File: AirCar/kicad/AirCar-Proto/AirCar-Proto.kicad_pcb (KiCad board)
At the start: 4 copper layers, 76.2 x 55.9 mm, 22 parts, among them J1 Conn_01x05, J2 Conn_01x20_Socket, J3 Conn_01x06, J4 PJ-102A, J5 Conn_01x20_Socket, SW2 SW_SPDT, U1 Pico, U2 LDL212PU50R, U3 TXU0104BQAR

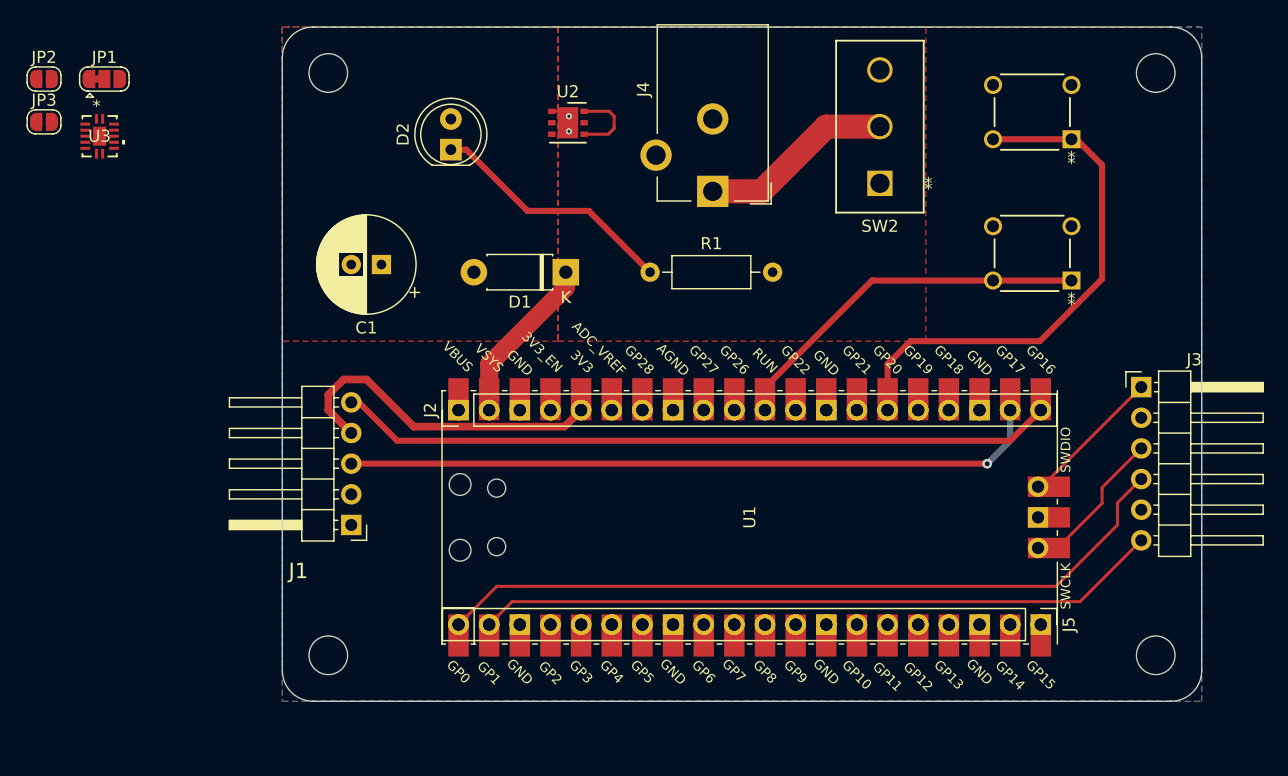
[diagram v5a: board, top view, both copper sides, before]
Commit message: switch to some none through hole parts because SMD is easier...
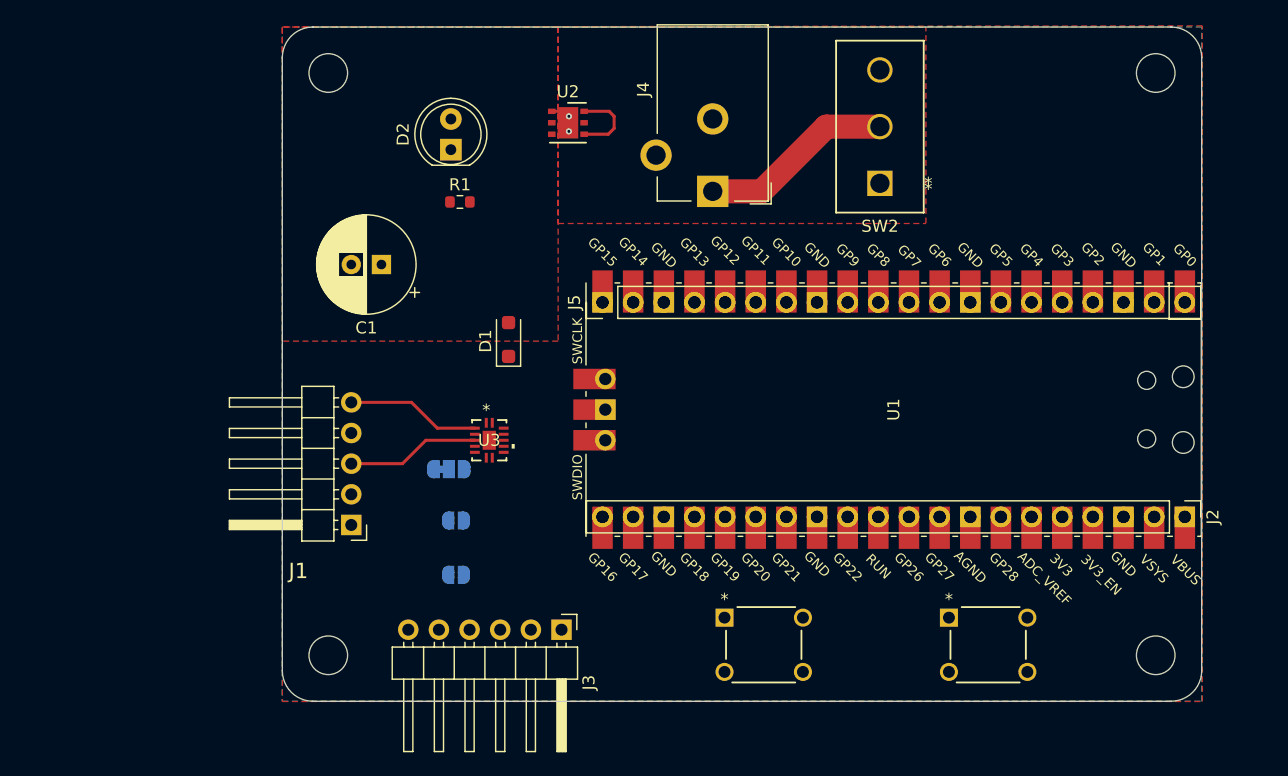
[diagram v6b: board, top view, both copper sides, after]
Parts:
- D1: footprint Diode_THT:D_DO-41_SOD81_P7.62mm_Horizontal -> Diode_SMD:D_SOD-123F
- JP1, JP2, JP3: moved to B.Cu
- R1: footprint Resistor_THT:R_Axial_DIN0207_L6.3mm_D2.5mm_P10.16mm_Horizontal -> Resistor_SMD:R_0603_1608Metric
- moved J2 60.8 mm to (138.3, 142.2), turned to -90 degrees
- moved J3 52.1 mm to (86.6, 151.6), turned to -90 degrees
- moved USER1 51.1 mm to (106.7, 155.1), turned to 0 degrees
- moved JP3 50.7 mm to (77.9, 147.0)
- moved JP2 50.0 mm to (77.9, 142.5)
- moved J5 45.1 mm to (90.0, 124.4), turned to 90 degrees
- moved JP1 43.1 mm to (77.3, 138.2)
- moved U3 41.0 mm to (80.7, 135.8)
- moved Reset1 37.0 mm to (125.3, 155.1), turned to 0 degrees
- moved R1 16.8 mm to (78.2, 116.1)
- moved U1 14.9 mm to (114.2, 133.3), turned to -90 degrees
- moved D1 7.32 mm to (82.2, 127.5), turned to 90 degrees
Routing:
- net /PicoTx: track 62.7 -> 0.00 mm
- net /PicoRx: track 56.9 -> 0.00 mm
- net /Lag: track 59.5 -> 11.1 mm
- net /Lead: track 57.9 -> 11.0 mm, vias 1 -> 0
- net Net-(J2-Pin_15): track 43.9 -> 0.00 mm
- net Net-(J2-Pin_11): track 30.9 -> 0.00 mm
- net (no net): track 27.6 -> 0.00 mm
- net Net-(D2-K): track 20.7 -> 0.00 mm
- net /VSYS: track 14.1 -> 0.00 mm
- net Net-(J3-Pin_3): track 12.7 -> 0.00 mm
- net Net-(J3-Pin_1): track 12.0 -> 0.00 mm
- added copper zone on F.Cu, net /VSYS
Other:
- copper layers 4 -> 2

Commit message: possible rev 0.1 candidate
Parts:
- removed J2, J5: Conn_01x20_Socket, Connector_PinHeader_2.54mm:PinHeader_1x20_P2.54mm_Vertical
- added C2: 0.1uF, Capacitor_SMD:C_0603_1608Metric, F.Cu at (77.3, 140.5)
- moved JP3 10.6 mm to (80.7, 136.8)
- moved JP2 9.17 mm to (80.7, 133.8)
- moved JP1 8.00 mm to (77.2, 130.2)
- moved J1 3.03 mm to (72.2, 142.9)
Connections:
- U1 pad 10: Net-(J5-Pin_11) -> unconnected-(U1-GPIO7-Pad10)
- U1 pad 11: Net-(J5-Pin_10) -> unconnected-(U1-GPIO8-Pad11)
- U1 pad 12: Net-(J5-Pin_9) -> unconnected-(U1-GPIO9-Pad12)
- U1 pad 14: Net-(J5-Pin_7) -> unconnected-(U1-GPIO10-Pad14)
- U1 pad 15: Net-(J5-Pin_6) -> unconnected-(U1-GPIO11-Pad15)
- U1 pad 16: Net-(J5-Pin_5) -> unconnected-(U1-GPIO12-Pad16)
- U1 pad 17: Net-(J5-Pin_4) -> unconnected-(U1-GPIO13-Pad17)
- U1 pad 19: Net-(J5-Pin_2) -> unconnected-(U1-GPIO14-Pad19)
- U1 pad 20: Net-(J5-Pin_1) -> unconnected-(U1-GPIO15-Pad20)
- U1 pad 24: Net-(J2-Pin_17) -> unconnected-(U1-GPIO18-Pad24)
- U1 pad 25: Net-(J2-Pin_16) -> unconnected-(U1-GPIO19-Pad25)
- U1 pad 27: Net-(J2-Pin_14) -> unconnected-(U1-GPIO21-Pad27)
- U1 pad 29: Net-(J2-Pin_12) -> unconnected-(U1-GPIO22-Pad29)
- U1 pad 31: Net-(J2-Pin_10) -> unconnected-(U1-GPIO26_ADC0-Pad31)
- U1 pad 32: Net-(J2-Pin_9) -> unconnected-(U1-GPIO27_ADC1-Pad32)
- U1 pad 34: Net-(J2-Pin_7) -> unconnected-(U1-GPIO28_ADC2-Pad34)
- U1 pad 35: Net-(J2-Pin_6) -> unconnected-(U1-ADC_VREF-Pad35)
- U1 pad 37: Net-(J2-Pin_4) -> unconnected-(U1-3V3_EN-Pad37)
- U1 pad 4: Net-(J5-Pin_17) -> unconnected-(U1-GPIO2-Pad4)
- U1 pad 40: Net-(J2-Pin_1) -> unconnected-(U1-VBUS-Pad40)
- U1 pad 5: Net-(J5-Pin_16) -> unconnected-(U1-GPIO3-Pad5)
- U1 pad 6: Net-(J5-Pin_15) -> unconnected-(U1-GPIO4-Pad6)
- U1 pad 7: Net-(J5-Pin_14) -> unconnected-(U1-GPIO5-Pad7)
- U1 pad 9: Net-(J5-Pin_12) -> unconnected-(U1-GPIO6-Pad9)
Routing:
- net /PicoRx: track 0.00 -> 82.3 mm, vias 0 -> 2
- net /PicoTx: track 0.00 -> 81.7 mm, vias 0 -> 3
- net /V3P3: track 0.00 -> 62.7 mm, vias 0 -> 3
- net Net-(J3-Pin_3): track 0.00 -> 26.0 mm
- net /Venc: track 0.00 -> 24.2 mm, vias 0 -> 2
- net /Lag_3P3: track 0.00 -> 20.2 mm, vias 0 -> 3
- net /Lead_3P3: track 0.00 -> 18.9 mm, vias 0 -> 2
- net Net-(J3-Pin_1): track 0.00 -> 18.6 mm
- net Net-(U1-RUN): track 0.00 -> 17.2 mm
- net Net-(U1-GPIO20): track 0.00 -> 14.9 mm
- net /V5p0: track 0.00 -> 4.64 mm, vias 0 -> 2
- net Net-(D2-K): track 0.00 -> 4.37 mm
- net GND: track 2.92 -> 6.88 mm, vias 2 -> 5
- net /Lead: track 11.0 -> 10.9 mm, vias 0 -> 1
- net /Lag: track 11.1 -> 11.0 mm, vias 0 -> 1
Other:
- board text added: "Clk"
- board text added: "Debug Port"
- board text added: "Gnd"
- board text added: "RESET"
- board text added: "Rx"
- board text added: "SWD"
- board text added: "To operate encoder at 3.3V 1) Depopulate U3 2) Cut trace on JP1 3) Bridge all 3 Jumpers"
- board text added: "Tx"
- board text added: "USER"

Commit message: Gerbers for initial proto
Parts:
- added G***: LOGO, Library:HW_V0.1, F.Cu at (153.6, 62.3)
- moved H2 55.7 mm to (164.0, 57.3)
- moved J3 55.7 mm to (114.8, 103.5)
- moved C1 55.7 mm to (99.8, 73.2)
- moved C2 55.7 mm to (105.4, 92.4)
- moved D1 55.7 mm to (110.4, 79.4)
- moved D2 55.7 mm to (105.6, 63.7)
- moved H3 55.7 mm to (164.0, 105.6)
- moved J1 55.7 mm to (100.4, 94.8)
- moved J4 55.7 mm to (127.3, 67.1)
- moved JP1 55.7 mm to (105.4, 82.2)
- moved JP2 55.7 mm to (108.8, 85.7)
- moved JP3 55.7 mm to (108.8, 88.7)
- moved Reset1 55.7 mm to (153.4, 107.0)
- moved SW2 55.7 mm to (141.2, 66.5)
- moved U1 55.7 mm to (142.3, 85.2)
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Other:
- board text added: "Air Car Mark II V0.1 Copyright 2023 Tad Truex"
